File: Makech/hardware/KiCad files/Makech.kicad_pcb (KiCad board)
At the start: 2 copper layers, 54.9 x 88.5 mm, 54 parts, among them IC1 ULN2803, J1 SWD, J2 USB_B_Micro, J3 ESP32-Exp, J4 Conn_02x05_Odd_Even, SW2 SW_DPDT_x2, U1 ATSAMD21G18A-AU, U2 CONN_01X04, U3 AP2114_3.3v, X1 Screw_Terminal_1x02

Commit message: pin reset move of gnd
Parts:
- J1: value SWD -> SWD programmer
- renumbered RESET to SW1
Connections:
- J3 pad 11: GND -> /ESP_RESET
- U1 pad 32: GND -> /ESP_RESET
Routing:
- net GND: track 85.5 -> 78.2 mm, vias 20 -> 19
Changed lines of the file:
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@@
-(kicad_pcb (version 20171130) (host pcbnew "(5.1.0)-1")
+(kicad_pcb (version 20171130) (host pcbnew "(5.1.2-1)-1")
   (general
     (thickness 1.6)
     (drawings 50)
-    (tracks 1213)
+    (tracks 1205)
     (zones 0)
     (modules 54)
-    (nets 67)
+    (nets 68)
   )
   (page A4)
@@
   (net 65 /D32)
   (net 66 /D36)
+  (net 67 /ESP_RESET)
   (net_class Default "This is the default net class."
     (clearance 0.2)
@@
     (add_net /ESP_MISO)
     (add_net /ESP_MOSI)
+    (add_net /ESP_RESET)
     (add_net /ESP_RTS)
     (add_net /ESP_SCK)
@@
       (net 57 /D2))
     (pad 32 smd rect (at 4.35 -0.75 90) (size 1.3 0.25) (layers F.Cu F.Paste F.Mask)
-      (net 1 GND))
+      (net 67 /ESP_RESET))
     (pad 33 smd rect (at 4.35 -1.25 90) (size 1.3 0.25) (layers F.Cu F.Paste F.Mask)
       (net 29 /D-))
@@
     (tags "SPST Tactile Switch")
     (attr smd)
-    (fp_text reference RESET (at -2.54 -3.75) (layer F.SilkS)
+    (fp_text reference SW1 (at -2.54 -3.75) (layer F.SilkS)
       (effects (font (size 1 1) (thickness 0.15)))
     )
@@
       (effects (font (size 0.77216 0.77216) (thickness 0.065024)) (justify left bottom mirror))
     )
-    (fp_text value SWD (at -3.13832 1.19404 180) (layer B.SilkS)
+    (fp_text value "SWD programmer" (at -3.13832 1.19404 180) (layer B.SilkS)
       (effects (font (size 0.77216 0.77216) (thickness 0.065024)) (justify left bottom mirror))
     )
@@
       (net 38 /ESP_SCK))
     (pad 11 smd rect (at 6.35 2.7) (size 3.1 1) (layers F.Cu F.Paste F.Mask)
-      (net 1 GND))
+      (net 67 /ESP_RESET))
     (pad 12 smd rect (at 6.35 -2.7) (size 3.1 1) (layers F.Cu F.Paste F.Mask)
       (net 39 /ESP_MISO))
@@
   (segment (start 131.1 68.36) (end 131.02 68.28) (width 0.3) (layer F.Cu) (net 1))
   (segment (start 131.1 69.31) (end 131.1 68.36) (width 0.3) (layer F.Cu) (net 1) (status 10))
-  (segment (start 132.6 70.26) (end 132.62 70.28) (width 0.3) (layer F.Cu) (net 1))
-  (segment (start 132.6 69.31) (end 132.6 70.26) (width 0.3) (layer F.Cu) (net 1) (status 10))
   (segment (start 137.7 73.91) (end 136.11 73.91) (width 0.3) (layer F.Cu) (net 1) (status 10))
   (segment (start 128.05 73.41) (end 127.72 73.08) (width 0.3) (layer F.Cu) (net 1))
@@
   (segment (start 132.68 76.72) (end 132.68 78.63) (width 0.3) (layer B.Cu) (net 1))
   (segment (start 132.199 82.541) (end 132.258043 82.600043) (width 0.5) (layer B.Cu) (net 1))
-  (segment (start 143.69 76.83) (end 142.525 75.665) (width 0.3) (layer F.Cu) (net 1) (status 10))
-  (segment (start 144.74 76.83) (end 143.69 76.83) (width 0.3) (layer F.Cu) (net 1) (status 30))
-  (via (at 142.625 73.2) (size 0.6) (drill 0.4) (layers F.Cu B.Cu) (net 1))
-  (segment (start 142.525 73.3) (end 142.625 73.2) (width 0.3) (layer F.Cu) (net 1))
-  (segment (start 142.525 75.665) (end 142.525 73.3) (width 0.3) (layer F.Cu) (net 1))
   (segment (start 131.1 69.31) (end 131.1 70.1) (width 0.3) (layer F.Cu) (net 1) (status 10))
   (segment (start 131.02 68.28) (end 131.02 67.54) (width 0.3) (layer F.Cu) (net 1))
@@
   (segment (start 131.02 67.54) (end 130.74 67.26) (width 0.3) (layer F.Cu) (net 1))
   (segment (start 131.65 70.65) (end 132.15 70.65) (width 0.3) (layer F.Cu) (net 1))
-  (segment (start 132.62 70.28) (end 132.62 71.43) (width 0.3) (layer F.Cu) (net 1))
   (segment (start 130.74 67.26) (end 130.74 66.62) (width 0.3) (layer F.Cu) (net 1))
   (segment (start 101.6 125.73) (end 103.15 125.73) (width 0.3) (layer B.Cu) (net 1) (status 10))

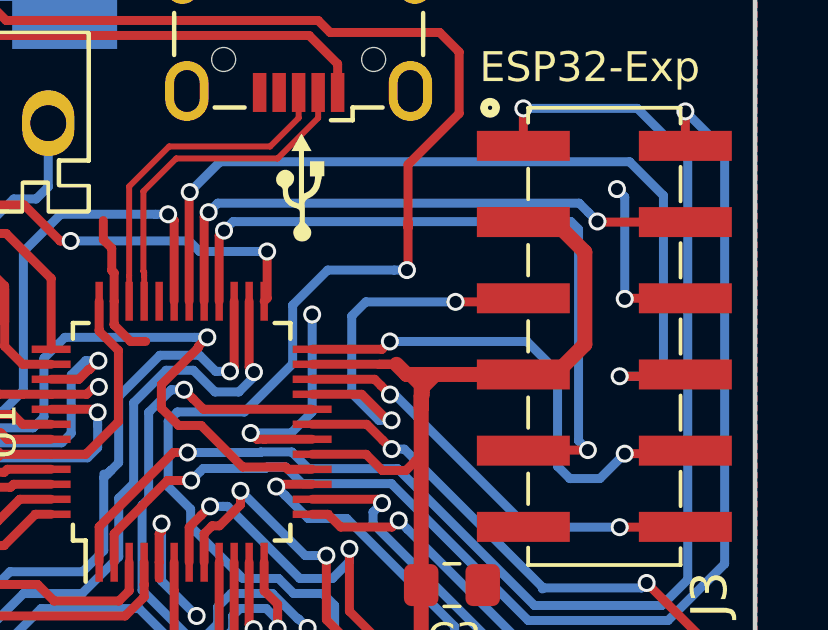
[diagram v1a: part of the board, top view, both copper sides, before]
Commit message: Remove CS tracks to voltage
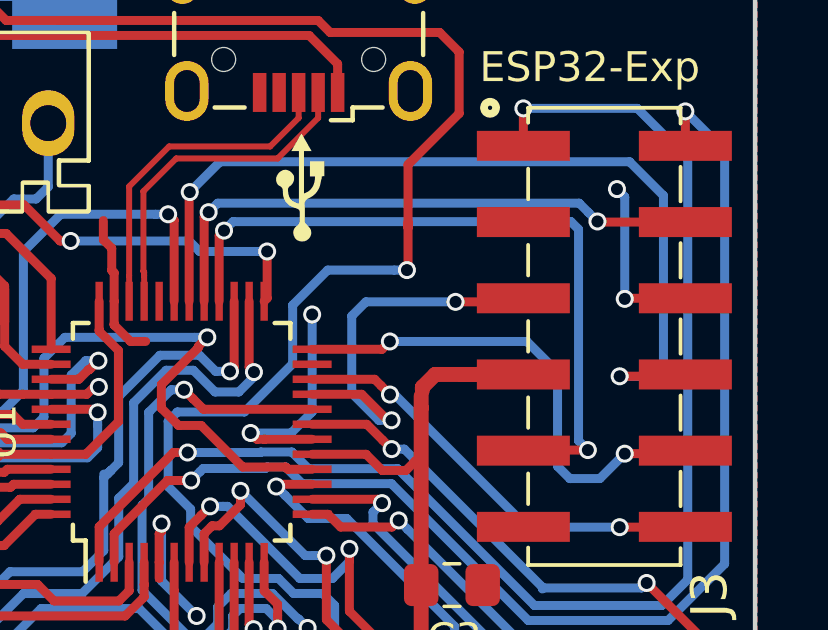
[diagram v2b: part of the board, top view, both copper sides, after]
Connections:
- J3 pad 3: +3V3 -> /ESP_CS
- U1 pad 23: +3V3 -> /ESP_CS
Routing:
- net +3V3: track 202.9 -> 188.8 mm
- net /ESP_CS: track 0.00 -> 1.05 mm
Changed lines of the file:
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@@
     (thickness 1.6)
     (drawings 50)
-    (tracks 1205)
+    (tracks 1191)
     (zones 0)
     (modules 54)
-    (nets 68)
+    (nets 69)
   )
   (page A4)
@@
   (net 66 /D36)
   (net 67 /ESP_RESET)
+  (net 68 /ESP_CS)
   (net_class Default "This is the default net class."
     (clearance 0.2)
@@
     (add_net /D9)
     (add_net /ESP_BUSY)
+    (add_net /ESP_CS)
     (add_net /ESP_GPIO)
     (add_net /ESP_MISO)
@@
       (net 39 /ESP_MISO))
     (pad 23 smd rect (at 2.25 4.35 180) (size 1.3 0.25) (layers F.Cu F.Paste F.Mask)
-      (net 6 +3V3))
+      (net 68 /ESP_CS))
     (pad 24 smd rect (at 2.75 4.35 180) (size 1.3 0.25) (layers F.Cu F.Paste F.Mask)
       (net 38 /ESP_SCK))
@@
       (net 32 /TX))
     (pad 3 smd rect (at -3.81 2.7) (size 3.1 1) (layers F.Cu F.Paste F.Mask)
-      (net 6 +3V3))
+      (net 68 /ESP_CS))
     (pad 2 smd rect (at -6.35 -2.7) (size 3.1 1) (layers F.Cu F.Paste F.Mask)
       (net 33 /RX))
@@
   (segment (start 131.554 81.446) (end 131.9 81.1) (width 0.5) (layer F.Cu) (net 6))
   (segment (start 131.554 82.804) (end 131.554 81.446) (width 0.5) (layer F.Cu) (net 6) (status 10))
-  (segment (start 137.7 71.41) (end 139.935 71.41) (width 0.3) (layer F.Cu) (net 6) (status 10))
-  (segment (start 139.935 71.41) (end 140.29 71.41) (width 0.3) (layer F.Cu) (net 6))
   (segment (start 133.1 78.01) (end 133.1 78.96) (width 0.3) (layer F.Cu) (net 6) (status 10))
   (segment (start 132.55 81.1) (end 133.1 80.55) (width 0.3) (layer F.Cu) (net 6))
   (segment (start 132.425 81.1) (end 132.55 81.1) (width 0.3) (layer F.Cu) (net 6))
   (segment (start 131.9 81.1) (end 132.425 81.1) (width 0.5) (layer F.Cu) (net 6))
-  (segment (start 141.375 72.275) (end 140.51 71.41) (width 0.3) (layer F.Cu) (net 6))
-  (segment (start 141.375 72.425) (end 141.375 72.275) (width 0.3) (layer F.Cu) (net 6))
-  (segment (start 139.935 71.41) (end 140.51 71.41) (width 0.3) (layer F.Cu) (net 6))
   (segment (start 105.2 83.98) (end 105.2 79.4) (width 0.5) (layer F.Cu) (net 6))
   (segment (start 131.554 82.804) (end 131.554 84.044) (width 0.5) (layer F.Cu) (net 6) (status 10))
@@
   (segment (start 136.23 94.3) (end 134.88 94.3) (width 0.5) (layer B.Cu) (net 6))
   (segment (start 137.0561 93.4739) (end 136.23 94.3) (width 0.5) (layer B.Cu) (net 6))
-  (segment (start 146.79 67.67) (end 145.79 66.67) (width 0.5) (layer F.Cu) (net 6) (status 20))
-  (segment (start 145.79 66.67) (end 144.74 66.67) (width 0.5) (layer F.Cu) (net 6) (status 30))
-  (segment (start 146.79 70.75) (end 146.79 67.67) (width 0.5) (layer F.Cu) (net 6))
-  (segment (start 145.79 71.75) (end 146.79 70.75) (width 0.5) (layer F.Cu) (net 6) (status 10))
+  (segment (start 145.79 66.67) (end 144.74 66.67) (width 0.5) (layer F.Cu) (net 68) (status 30))
   (segment (start 144.74 71.75) (end 145.79 71.75) (width 0.5) (layer F.Cu) (net 6) (status 30))
   (via (at 110.25 94.3) (size 0.6) (drill 0.4) (layers F.Cu B.Cu) (net 6))
@@
   (segment (start 141.335 83.24) (end 141.335 78.77) (width 0.5) (layer F.Cu) (net 6) (status 20))
   (segment (start 140.045 84.53) (end 141.335 83.24) (width 0.5) (layer F.Cu) (net 6))
-  (segment (start 141.375 72.425) (end 141.335 72.465) (width 0.5) (layer F.Cu) (net 6))
-  (segment (start 140.85 71.75) (end 140.51 71.41) (width 0.5) (layer F.Cu) (net 6))
-  (segment (start 141.335 71.91) (end 141.175 71.75) (width 0.5) (layer F.Cu) (net 6))
-  (segment (start 141.335 72.865) (end 141.335 71.91) (width 0.5) (layer F.Cu) (net 6))
-  (segment (start 141.175 71.75) (end 140.85 71.75) (width 0.5) (layer F.Cu) (net 6))
   (segment (start 141.335 72.465) (end 141.335 72.865) (width 0.5) (layer F.Cu) (net 6))
   (segment (start 141.335 72.865) (end 141.335 78.77) (width 0.5) (layer F.Cu) (net 6) (status 20))
   (segment (start 141.375 72.175) (end 141.8 71.75) (width 0.5) (layer F.Cu) (net 6))
   (segment (start 141.375 72.275) (end 141.375 72.175) (width 0.5) (layer F.Cu) (net 6))
-  (segment (start 141.8 71.75) (end 141.175 71.75) (width 0.5) (layer F.Cu) (net 6))
   (segment (start 144.74 71.75) (end 141.8 71.75) (width 0.5) (layer F.Cu) (net 6) (status 10))
   (segment (start 138.78 84.53) (end 140.045 84.53) (width 0.5) (layer F.Cu) (net 6))

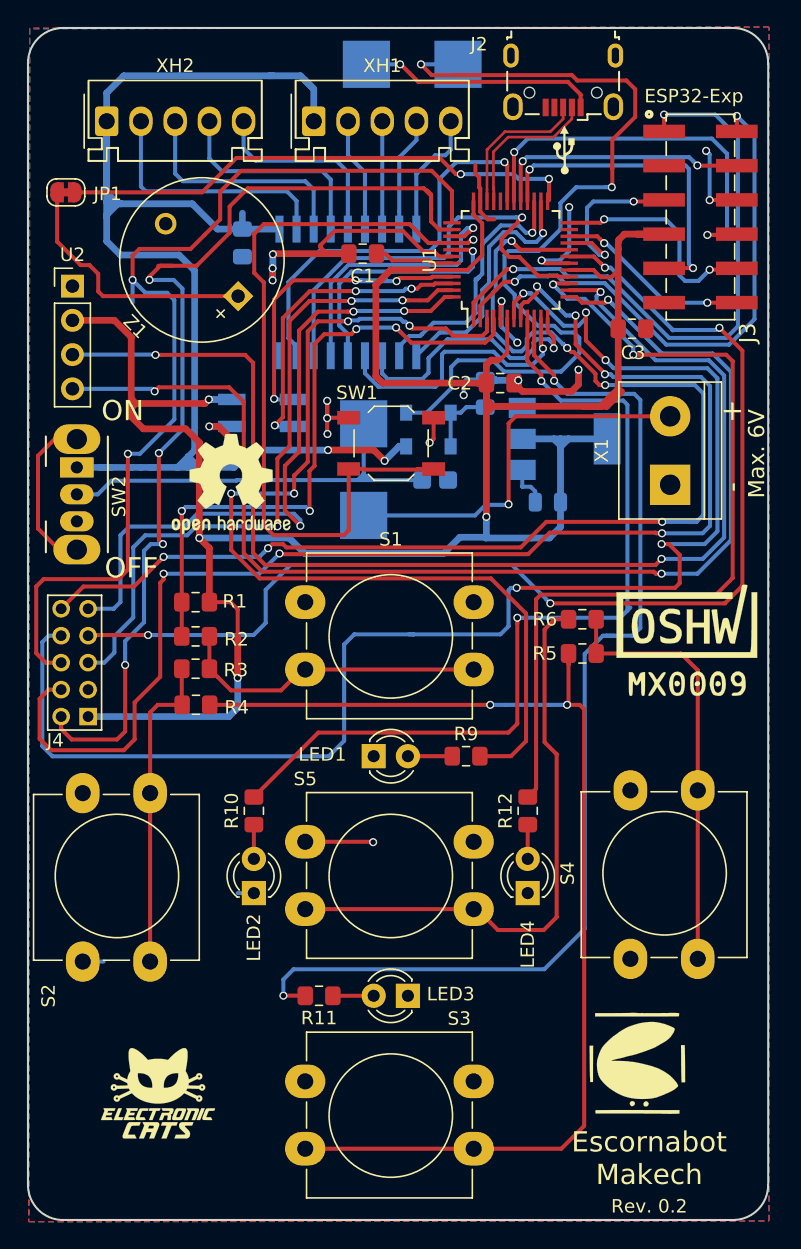
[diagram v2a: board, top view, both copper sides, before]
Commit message: Update connector  to 2.54mm and fix traces and ground plane
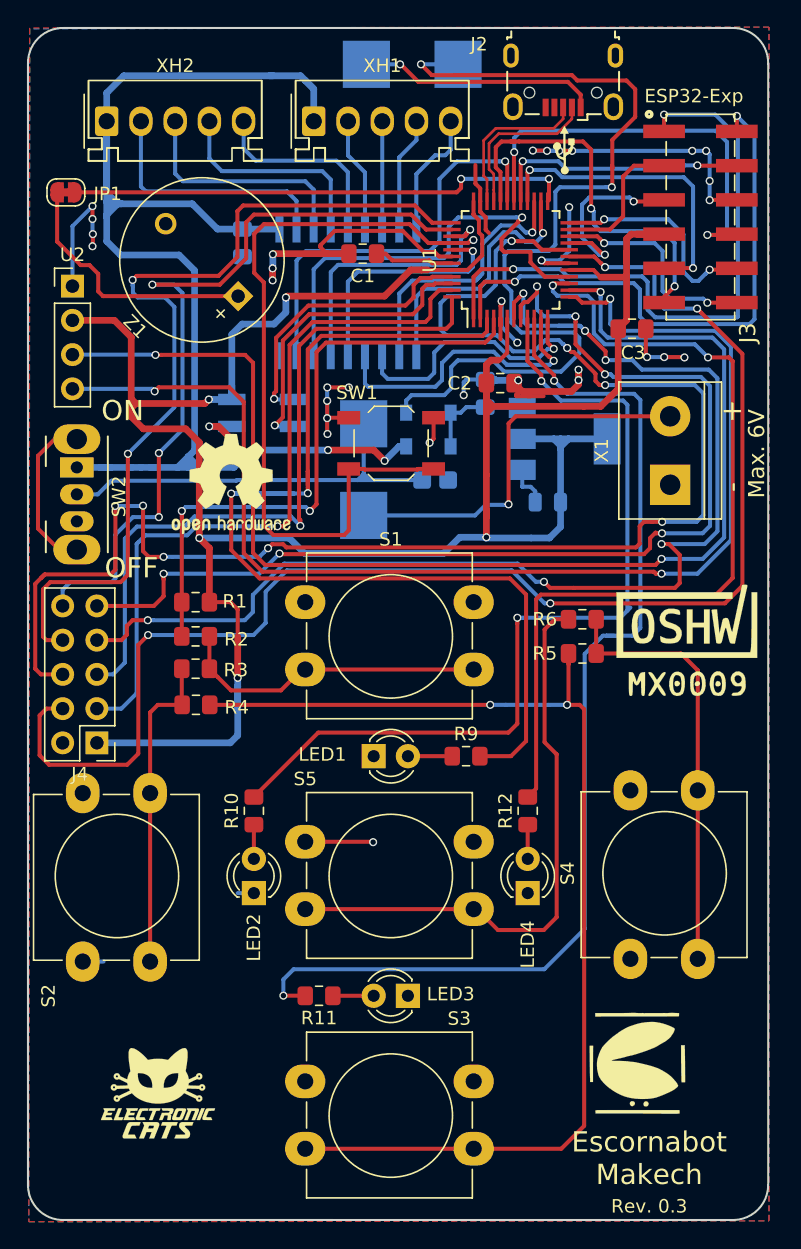
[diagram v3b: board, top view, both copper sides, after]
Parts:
- J4: footprint Pines:62001021121 -> Connector_PinHeader_2.54mm:PinHeader_2x05_P2.54mm_Vertical
- moved J4 6.17 mm to (102.7, 109.5), turned to 180 degrees
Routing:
- net GND: track 78.2 -> 118.8 mm, vias 19 -> 35
- net /ESP_RESET: track 0.00 -> 28.9 mm, vias 0 -> 2
- net /D34: track 91.2 -> 116.0 mm, vias 6 -> 8
- net /D31: track 109.5 -> 89.5 mm, vias 5 -> 6
- net /D33: track 87.3 -> 105.1 mm
- net /D36: track 76.0 -> 58.7 mm, vias 4 -> 3
- net /D32: track 98.5 -> 81.4 mm
- net /ESP_CS: track 1.05 -> 11.8 mm
- net /D35: track 74.1 -> 66.1 mm
- net +3V3: track 188.8 -> 194.2 mm, vias 4 -> 5
- net /A0: track 73.8 -> 79.1 mm, vias 4 -> 2
- net /D6: track 21.4 -> 25.3 mm
- net /SWCLK: track 25.1 -> 21.5 mm, vias 3 -> 1
- net /D29: track 50.6 -> 54.1 mm, vias 3 -> 1
- net /D30: track 50.1 -> 53.1 mm, vias 3 -> 1
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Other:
- board text added: "Rev. 0.3"

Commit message: Update traces fix ground missed
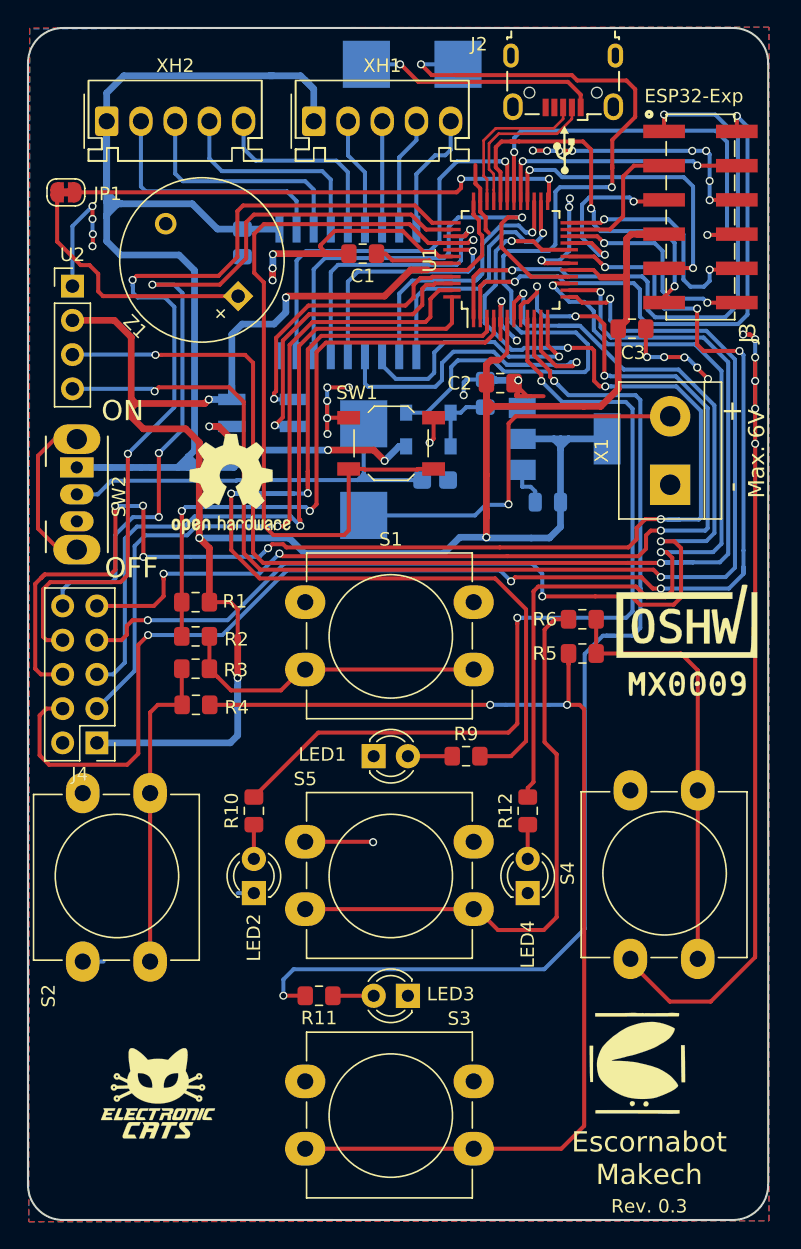
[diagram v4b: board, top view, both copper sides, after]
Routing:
- net GND: track 118.8 -> 177.4 mm, vias 35 -> 42
- net /D34: track 116.0 -> 109.7 mm
- net /SCL: track 93.1 -> 98.8 mm
- net /D6: track 25.3 -> 29.1 mm
- net /SDA: track 91.6 -> 93.8 mm
- net VCC: track 70.4 -> 71.7 mm
- net /ESP_SCK: track 16.5 -> 17.6 mm
- net /D29: track 54.1 -> 53.0 mm
- net /RX: track 42.6 -> 41.7 mm
- net /A0: track 79.1 -> 78.5 mm
- net /D31: track 89.5 -> 90.1 mm, vias 6 -> 4
- net /TX: track 46.4 -> 45.9 mm
- net /D33: track 105.1 -> 104.7 mm, vias 4 -> 6

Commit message: update v3
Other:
- board text removed: "Rev. 0.2"
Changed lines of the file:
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@@
-(kicad_pcb (version 20171130) (host pcbnew "(5.1.0-0)")
+(kicad_pcb (version 20171130) (host pcbnew "(5.1.2-1)-1")
   (general
     (thickness 1.6)
@@
     (43 Eco2.User user)
     (44 Edge.Cuts user)
-    (45 Margin user hide)
+    (45 Margin user)
     (46 B.CrtYd user hide)
     (47 F.CrtYd user hide)
@@
     (visible_elements 7FFFFFFF)
     (pcbplotparams
-      (layerselection 0x010f0_80000001)
+      (layerselection 0x010fc_ffffffff)
       (usegerberextensions true)
       (usegerberattributes false)
@@
       (drillshape 0)
       (scaleselection 1)
-      (outputdirectory "../Gerber/"))
+      (outputdirectory "../escorna_v3/"))
   )
   (net 0 "")
@@
     (effects (font (size 1.5 1.5) (thickness 0.3)))
   )
-  (gr_text "Rev. 0.2" (at 143.58112 143.8402) (layer B.SilkS)
+  (gr_text "Rev. 0.3" (at 143.58112 143.8402) (layer B.SilkS)
     (effects (font (size 1 1) (thickness 0.25)) (justify mirror))
   )
